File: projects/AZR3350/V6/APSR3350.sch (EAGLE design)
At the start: 214 parts, among them IC1 A4403, IC10 A4988, IC2 LDO-TS1117CW-3V3, IC3 ATSAM4S8C, IC4 74AHC08, IC7 A4988, IC8 A4988, IC9 A4988, J1 ZX62-AB-5PA, J2 MOLEX-SD-47571-001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

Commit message: More progress
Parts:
- RESET: value (none) -> EVQP7J; device misc:EVQQ2 -> misc:EVQP7J
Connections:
- removed net PWR_FAIL_DET: IC3.PC12/AD12
- net E_STOP: now also IC3.PA7/XIN32/PGMNVALID; no longer IC3.PC17
- net LCD_CS: now also IC4D.I0; no longer IC4D.I1
- net LCD_SCK: now also IC4D.I1; no longer IC4D.I0
- net PWR_FAIL_DET2: now also IC3.PC12/AD12
- net X_STOP: now also IC3.PC15/AD11; no longer IC3.TMS/SWDIO/PB6
- net Y_STOP: now also IC3.PA23/PGMD11; no longer IC3.PC18
- net Z_EN: now also IC3.TDI/PB4; no longer IC3.PA7/XIN32/PGMNVALID
- net Z_STOP: now also IC3.PC9; no longer IC3.TDO/TRACESWO/PB5
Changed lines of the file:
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@@
 <?xml version="1.0" encoding="utf-8"?>
 <!DOCTYPE eagle SYSTEM "eagle.dtd">
-<eagle version="9.5.0">
+<eagle version="9.5.1">
 <drawing>
 <settings>
@@
 <part name="C38" library="resistor" library_urn="urn:adsk.eagle:library:348" deviceset="C-EU" device="C0603" package3d_urn="urn:adsk.eagle:package:23616/2" value="100n"/>
 <part name="+3V5" library="supply1" library_urn="urn:adsk.eagle:library:371" deviceset="+3V3" device=""/>
-<part name="RESET" library="misc" deviceset="EVQQ2" device=""/>
+<part name="RESET" library="misc" deviceset="EVQP7J" device=""/>
 <part name="GND27" library="supply1" library_urn="urn:adsk.eagle:library:371" deviceset="GND" device=""/>
 <part name="F1" library="misc" deviceset="MC36207" device=""/>
@@
 </segment>
 <segment>
-<pinref part="IC3" gate="G$1" pin="TMS/SWDIO/PB6"/>
-<wire x1="-612.14" y1="193.04" x2="-591.82" y2="193.04" width="0.1524" layer="91" grouprefs="MICROCONTROLLER"/>
-<label x="-609.6" y="193.04" size="1.778" layer="95" grouprefs="MICROCONTROLLER"/>
+<pinref part="IC3" gate="G$1" pin="PC15/AD11"/>
+<wire x1="-734.06" y1="200.66" x2="-713.74" y2="200.66" width="0.1524" layer="91"/>
+<label x="-734.06" y="200.66" size="1.778" layer="95"/>
 </segment>
 </net>
@@
 </segment>
 <segment>
-<pinref part="IC3" gate="G$1" pin="PC18"/>
-<wire x1="-612.14" y1="190.5" x2="-591.82" y2="190.5" width="0.1524" layer="91" grouprefs="MICROCONTROLLER"/>
-<label x="-609.6" y="190.5" size="1.778" layer="95" grouprefs="MICROCONTROLLER"/>
+<pinref part="IC3" gate="G$1" pin="PA23/PGMD11"/>
+<wire x1="-713.74" y1="193.04" x2="-734.06" y2="193.04" width="0.1524" layer="91"/>
+<label x="-734.06" y="193.04" size="1.778" layer="95"/>
 </segment>
 </net>
@@
 <net name="Z_STOP" class="0">
 <segment>
-<pinref part="IC3" gate="G$1" pin="TDO/TRACESWO/PB5"/>
-<wire x1="-612.14" y1="185.42" x2="-591.82" y2="185.42" width="0.1524" layer="91" grouprefs="MICROCONTROLLER"/>
-<label x="-609.6" y="185.42" size="1.778" layer="95" grouprefs="MICROCONTROLLER"/>
-</segment>
-<segment>
 <pinref part="R77" gate="G$1" pin="1"/>
 <wire x1="-294.64" y1="220.98" x2="-302.26" y2="220.98" width="0.1524" layer="91" grouprefs="ENDSTOPS"/>
@@
 <junction x="-314.96" y="220.98" grouprefs="ENDSTOPS"/>
 </segment>
+<segment>
+<pinref part="IC3" gate="G$1" pin="PC9"/>
+<wire x1="-612.14" y1="154.94" x2="-591.82" y2="154.94" width="0.1524" layer="91"/>
+<label x="-609.6" y="154.94" size="1.778" layer="95"/>
+</segment>
 </net>
 <net name="FAN1" class="0">
@@
 </segment>
 <segment>
-<pinref part="IC3" gate="G$1" pin="PA7/XIN32/PGMNVALID"/>
-<wire x1="-713.74" y1="134.62" x2="-734.06" y2="134.62" width="0.1524" layer="91"/>
-<label x="-734.06" y="134.62" size="1.778" layer="95"/>
+<pinref part="IC3" gate="G$1" pin="TDI/PB4"/>
+<wire x1="-612.14" y1="129.54" x2="-591.82" y2="129.54" width="0.1524" layer="91"/>
+<label x="-609.6" y="129.54" size="1.778" layer="95"/>
 </segment>
 </net>
@@
 <wire x1="-20.32" y1="172.72" x2="-17.78" y2="172.72" width="0.1524" layer="91" grouprefs="LCD"/>
 <junction x="-20.32" y="190.5" grouprefs="LCD"/>
-<wire x1="-20.32" y1="172.72" x2="-20.32" y2="154.94" width="0.1524" layer="91" grouprefs="LCD"/>
-<wire x1="-20.32" y1="154.94" x2="-17.78" y2="154.94" width="0.1524" layer="91" grouprefs="LCD"/>
+<wire x1="-20.32" y1="172.72" x2="-20.32" y2="160.02" width="0.1524" layer="91" grouprefs="LCD"/>
+<wire x1="-20.32" y1="160.02" x2="-17.78" y2="160.02" width="0.1524" layer="91" grouprefs="LCD"/>
 <junction x="-20.32" y="172.72" grouprefs="LCD"/>
 <pinref part="IC4" gate="B" pin="I0"/>
 <pinref part="IC4" gate="B" pin="I1"/>
 <pinref part="IC4" gate="C" pin="I1"/>
-<pinref part="IC4" gate="D" pin="I1"/>
+<pinref part="IC4" gate="D" pin="I0"/>
 </segment>
 <segment>
@@
 </segment>
 <segment>
-<wire x1="-17.78" y1="160.02" x2="-38.1" y2="160.02" width="0.1524" layer="91" grouprefs="LCD"/>
-<label x="-38.1" y="160.02" size="1.778" layer="95" grouprefs="LCD"/>
-<pinref part="IC4" gate="D" pin="I0"/>
+<wire x1="-17.78" y1="154.94" x2="-38.1" y2="154.94" width="0.1524" layer="91" grouprefs="LCD"/>
+<label x="-38.1" y="154.94" size="1.778" layer="95" grouprefs="LCD"/>
+<pinref part="IC4" gate="D" pin="I1"/>
 </segment>
 </net>
@@
 </segment>
 </net>
-<net name="PWR_FAIL_DET" class="0">
-<segment>
-<pinref part="IC3" gate="G$1" pin="PC12/AD12"/>
-<wire x1="-713.74" y1="190.5" x2="-734.06" y2="190.5" width="0.1524" layer="91" grouprefs="MICROCONTROLLER"/>
-<label x="-734.06" y="190.5" size="1.778" layer="95" grouprefs="MICROCONTROLLER"/>
-</segment>
-</net>
 <net name="VSSA_MON" class="0">
 <segment>
@@
 <net name="E_STOP" class="0">
 <segment>
-<pinref part="IC3" gate="G$1" pin="PC17"/>
-<wire x1="-612.14" y1="182.88" x2="-591.82" y2="182.88" width="0.1524" layer="91" grouprefs="MICROCONTROLLER"/>
-<label x="-609.6" y="182.88" size="1.778" layer="95" grouprefs="MICROCONTROLLER"/>
-</segment>
-<segment>
 <label x="-337.82" y="205.74" size="1.778" layer="95" grouprefs="ENDSTOPS"/>
 <wire x1="-337.82" y1="205.74" x2="-314.96" y2="205.74" width="0.1524" layer="91" grouprefs="ENDSTOPS"/>
@@
 <junction x="-314.96" y="205.74" grouprefs="ENDSTOPS"/>
 </segment>
+<segment>
+<pinref part="IC3" gate="G$1" pin="PA7/XIN32/PGMNVALID"/>
+<wire x1="-713.74" y1="134.62" x2="-734.06" y2="134.62" width="0.1524" layer="91"/>
+<label x="-734.06" y="134.62" size="1.778" layer="95"/>
+</segment>
 </net>
 <net name="E_STOP_IN" class="0">
@@
 <junction x="-1191.26" y="182.88" grouprefs="POWER"/>
 </segment>
+<segment>
+<pinref part="IC3" gate="G$1" pin="PC12/AD12"/>
+<wire x1="-713.74" y1="190.5" x2="-734.06" y2="190.5" width="0.1524" layer="91" grouprefs="MICROCONTROLLER"/>
+<label x="-734.06" y="190.5" size="1.778" layer="95" grouprefs="MICROCONTROLLER"/>
+</segment>
 </net>

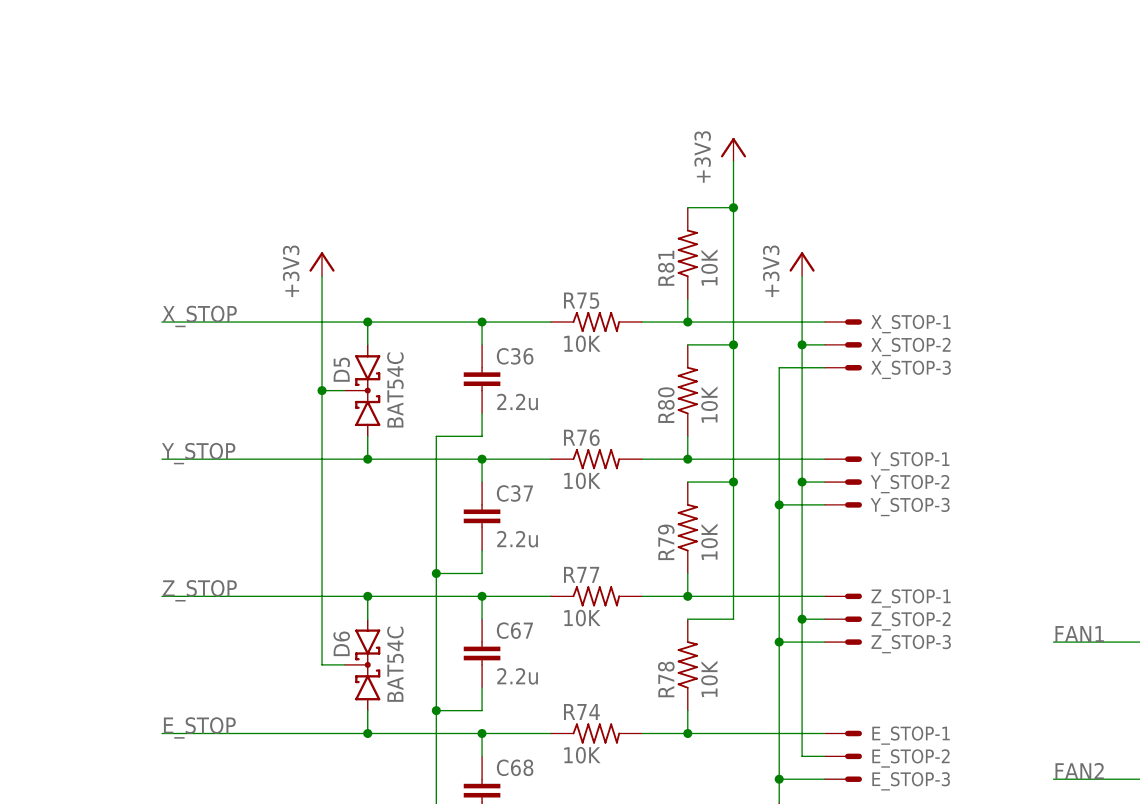
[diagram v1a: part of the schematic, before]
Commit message: All placed and routed
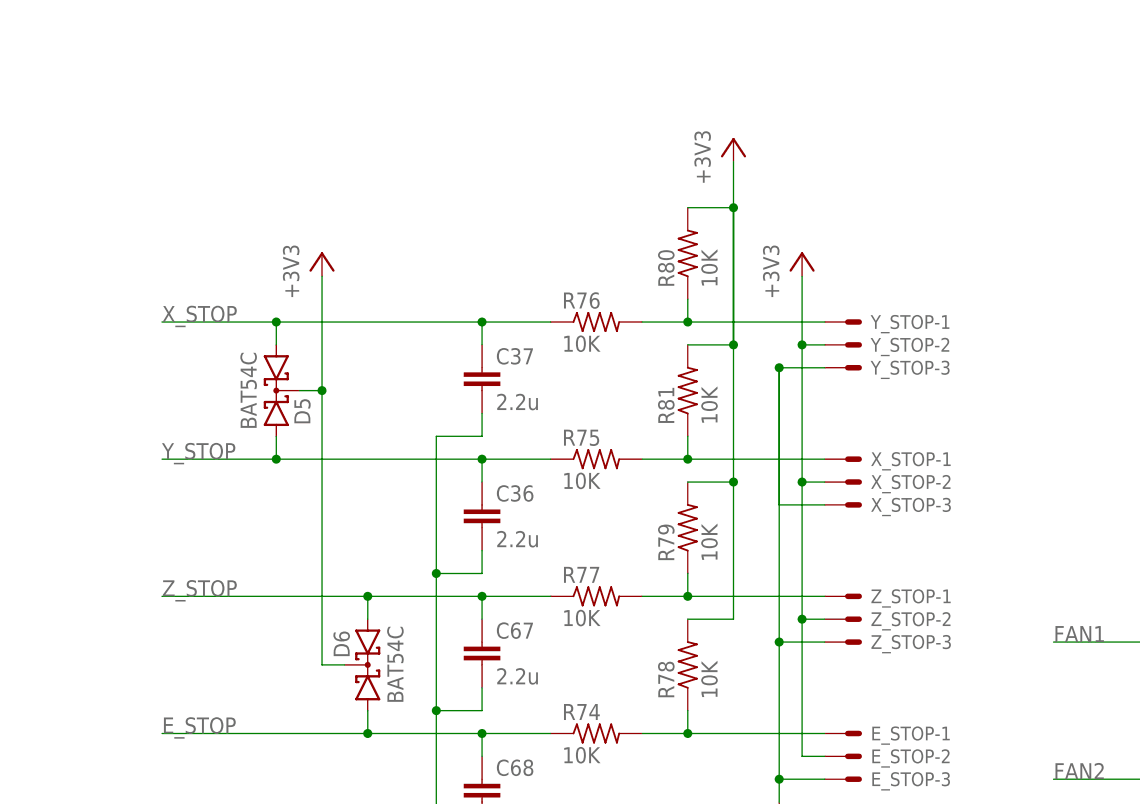
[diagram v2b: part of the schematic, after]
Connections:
- net X_STOP: now also C37.1, D5.A1, R76.1; no longer C36.1, D5.A2, R75.1
- net X_STOP_IN: now also R76.2, R80.1, Y_STOP-1.S; no longer R75.2, R81.1, X_STOP-1.S
- net Y_STOP: now also C36.1, D5.A2, R75.1; no longer C37.1, D5.A1, R76.1
- net Y_STOP_IN: now also R75.2, R81.1, X_STOP-1.S; no longer R76.2, R80.1, Y_STOP-1.S
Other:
- moved on the sheet: C36, C37, D5, R75, R76, R80, R81, X_STOP-1, X_STOP-2, X_STOP-3, Y_STOP-1, Y_STOP-2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

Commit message: Minor improvements, cam
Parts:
- renumbered ES1 to ESP8266, JP2 to J4, JP3 to J5, SG1 to BEEPER
